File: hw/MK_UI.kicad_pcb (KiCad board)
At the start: 2 copper layers, 35 parts, among them J1 Conn_01x20-FFC, J2 UI 20-Ribbon, J3 SW_MATRIX-Conn, SW1 UP, SW2 LF, SW3 EN, SW4 RT, SW5 DN

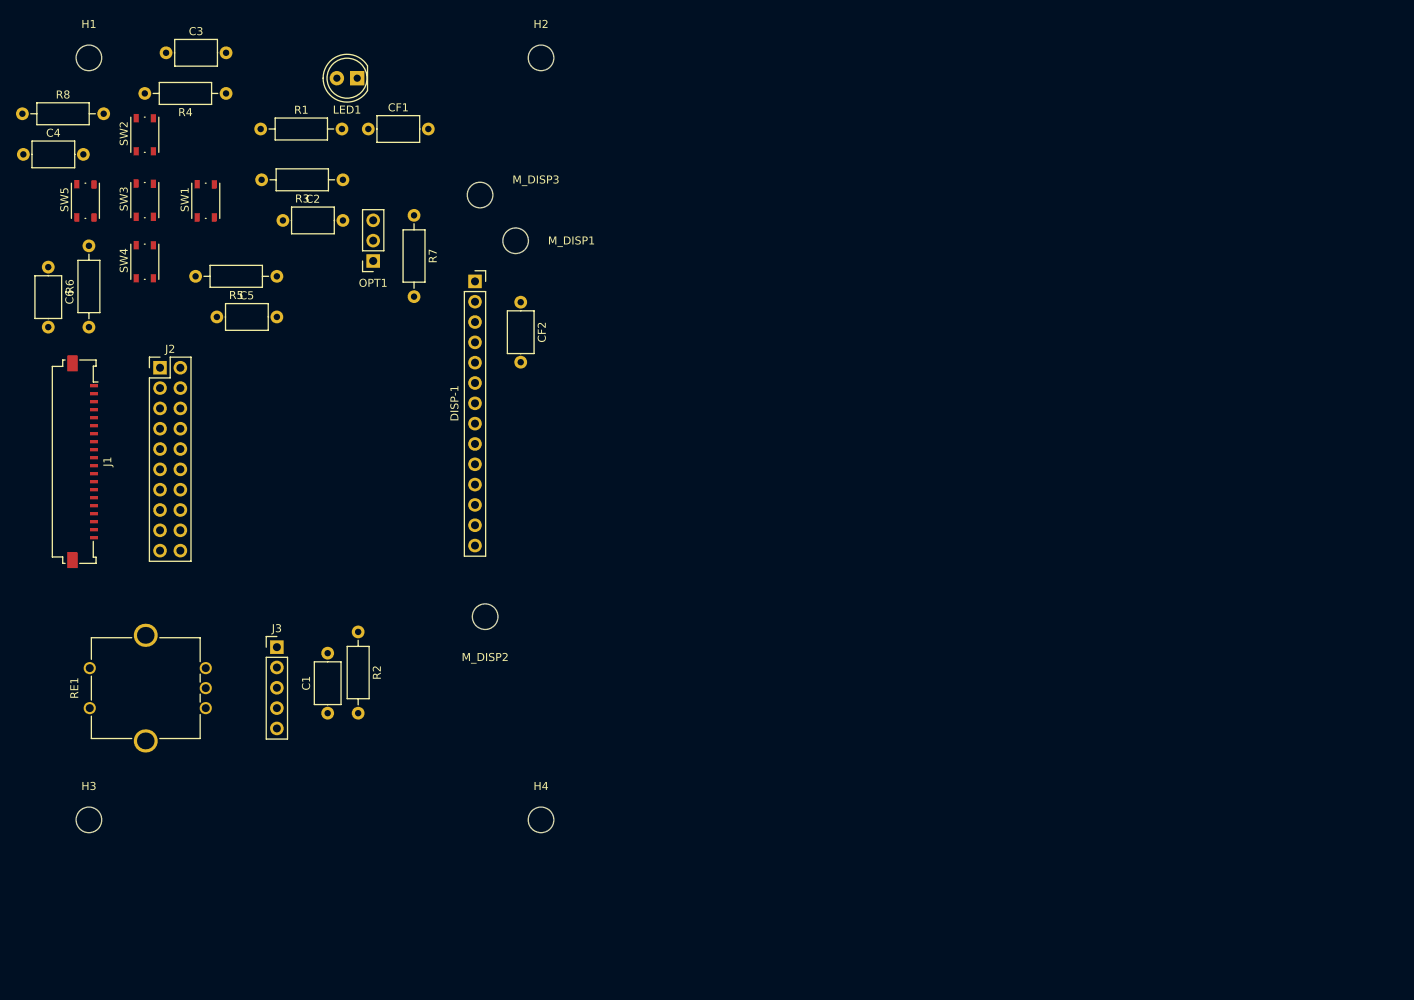
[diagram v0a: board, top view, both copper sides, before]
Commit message: Device (Main) and K&S-IF ready for layout.
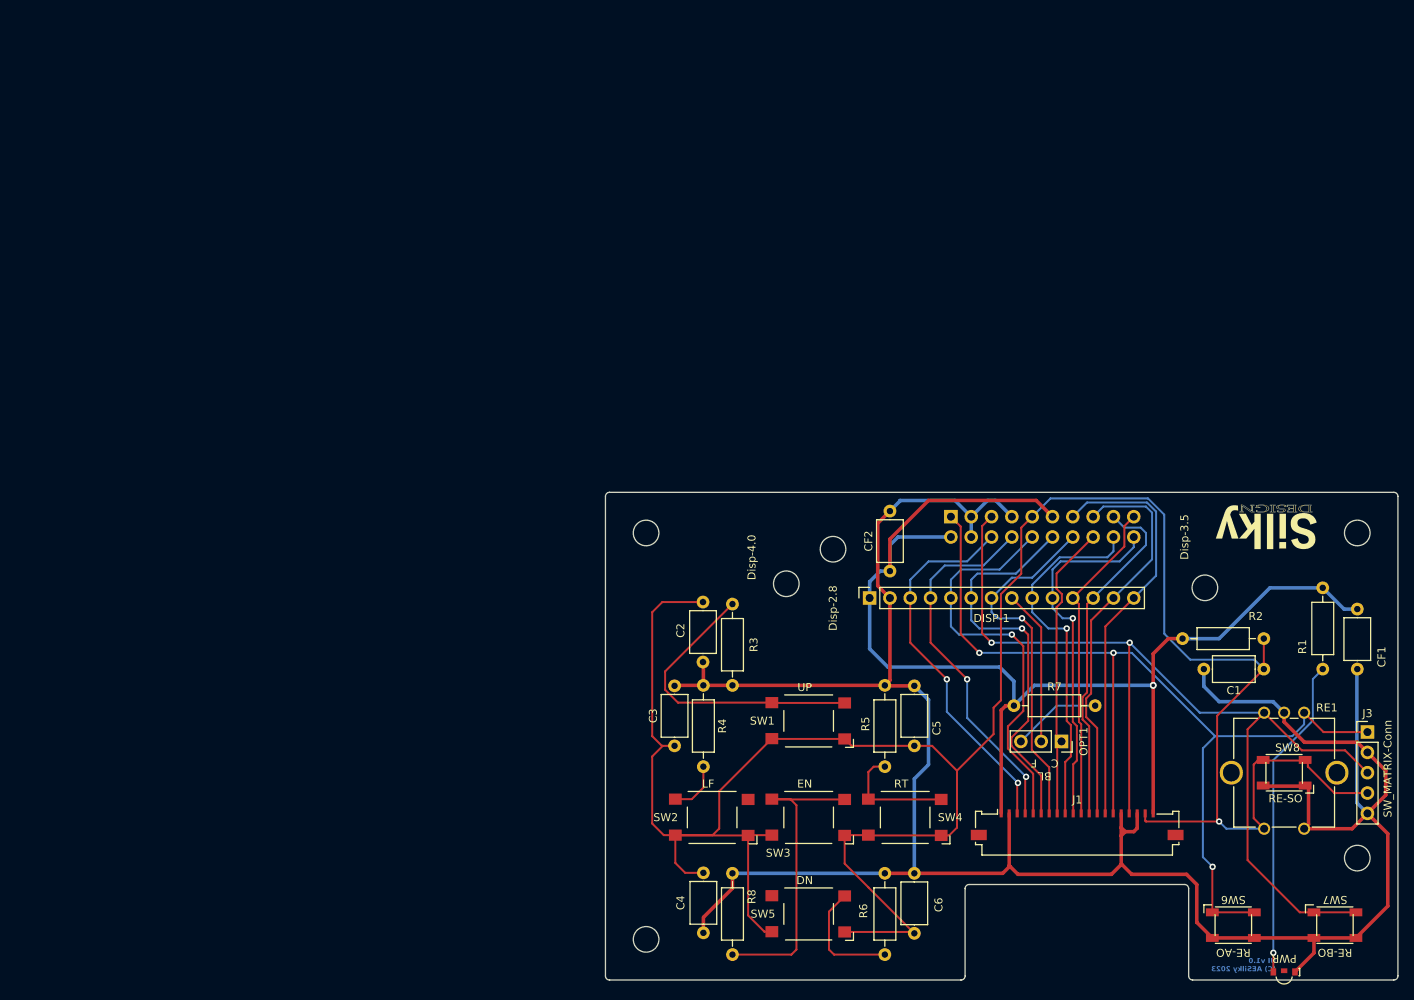
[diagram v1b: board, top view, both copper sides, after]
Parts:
- added G***: LOGO, AES_Library:SILKY-DESIGN-logo-0_50-AES, F.Cu at (200.5, 100.5)
- added G***: LOGO, AES_Library:SILKY-DESIGN-logo-0_50-AES, B.Cu at (209.9, 153.4)
- added SW6: RE-AO, AES_Library:SW_PUSH_SMD_1P1T_NO_45x45mm-CK, F.Cu at (196.4, 150.3)
- added SW7: RE-BO, AES_Library:SW_PUSH_SMD_1P1T_NO_45x45mm-CK, F.Cu at (209.1, 150.3)
- added SW8: RE-SO, AES_Library:SW_PUSH_SMD_1P1T_NO_45x45mm-CK, F.Cu at (202.7, 131.3)
- J2: value UI 20-Ribbon -> UI 20-RBN; moved to B.Cu
- LED1: footprint LED_THT:LED_D5.0mm -> AES_Library:LED_SMD_SIDEVIEW_Harvatek
- M_DISP1: value MountingHole-2_8 -> Disp-2.8
- M_DISP2: value MountingHole-3_5 -> Disp-3.5
- M_DISP3: value MountingHole-4_0 -> Disp-4.0
- SW1, SW2, SW3, SW4, SW5: footprint Button_Switch_SMD:SW_Push_1P1T_NO_Vertical_Wuerth_434133025816 -> AES_Library:SW_PUSH_SMD_1P1T_NO_6x6mm
- moved LED1 161.3 mm to (202.7, 156.7), turned to -90 degrees
- moved H3 158.6 mm to (211.9, 141.9), turned to 90 degrees
- moved R1 144.6 mm to (207.6, 108.2), turned to -90 degrees
- moved CF1 137.4 mm to (211.9, 110.8), turned to -90 degrees
- moved RE1 137.3 mm to (205.2, 123.8), turned to -90 degrees
- moved J3 136.7 mm to (213.2, 126.2)
- moved C6 136.6 mm to (156.5, 151.3), turned to 90 degrees
- moved J1 131.7 mm to (176.9, 137.3), turned to 0 degrees
- moved H1 130.4 mm to (123.0, 152.1), turned to 90 degrees
- moved R8 130.0 mm to (133.8, 143.8), turned to -90 degrees
- moved SW5 127.0 mm to (143.3, 148.9), turned to 180 degrees
- moved C4 123.7 mm to (130.1, 143.8), turned to -90 degrees
- moved R6 120.7 mm to (152.8, 143.8), turned to -90 degrees
- moved SW4 117.7 mm to (155.4, 136.9), turned to 180 degrees
- moved C1 117.1 mm to (200.2, 118.3), turned to 180 degrees
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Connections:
- J1 pad 10: /SD_TP_EX_SCK -> /TCH_CLK
- J1 pad 12: /SD_TP_EX_MOSI -> /TCH_MOSI
- J1 pad 13: /SD_TP_EX_MISO -> /TCH_MISO
- J2 pad 13: /TCH_CS- -> /TCH_IRQ-
- J2 pad 15: /SD_TP_EX_MOSI -> /TCH_MISO
- J2 pad 17: /SD_TP_EX_MISO -> /TCH_MOSI
- J2 pad 19: /TCH_IRQ- -> /TCH_CS-
- J2 pad 20: /SD_TP_EX_SCK -> /TCH_CLK
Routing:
- net /SW_MTRX: track 0.00 -> 312.9 mm, vias 0 -> 1
- net GND: track 0.00 -> 312.2 mm
- net +3.3V: track 0.00 -> 155.8 mm, vias 0 -> 1
- net /RE_B: track 0.00 -> 127.3 mm, vias 0 -> 2
- net /RE_A: track 0.00 -> 123.1 mm, vias 0 -> 3
- net /TCH_IRQ-: track 0.00 -> 52.0 mm
- net /DISP_D/C-: track 0.00 -> 51.3 mm, vias 0 -> 1
- net /DISP_MOSI: track 0.00 -> 50.1 mm, vias 0 -> 1
- net /TCH_MISO: track 0.00 -> 49.8 mm
- net /DISP_CS-: track 0.00 -> 47.2 mm, vias 0 -> 2
- net /DISP_RST-: track 0.00 -> 46.6 mm, vias 0 -> 2
- net /DISP_MISO: track 0.00 -> 45.9 mm, vias 0 -> 1
- net /TCH_CLK: track 0.00 -> 45.3 mm, vias 0 -> 1
- net /DISP_SCK: track 0.00 -> 45.0 mm, vias 0 -> 1
- net /TCH_MOSI: track 0.00 -> 43.6 mm
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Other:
- board outline added: 99.1 x 61 mm
- board text added: "BL C F"
- board text added: "UI v1.0 (C) AESilky 2023"
